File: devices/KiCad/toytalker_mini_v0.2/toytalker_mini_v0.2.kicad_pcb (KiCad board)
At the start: 2 copper layers, 40 x 40 mm, 38 parts, among them J1 TYPE-C-31-M-12, J2 SM02B-SRSS-TB(LF)(SN), U1 BQ25185DLHR, U2 AP2112K-3.3TRG1, U3 ESP32-S3-MINI-1-N4R2, U4 MAX98357AEWL_T

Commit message: Import v0.2 schematic changes into PCB and remove stale v0.1 footprints
- Update board from schematic: new connectors (ZH battery, MX1.25 speaker,
  MSK12C02 slide switch), thermistors TH1/TH2, new passives R9-R14/C10/C11
- Remove 4 ghost footprints left from v0.1: old SH connectors (J2/SP1),
  old SSAJ110100 switch, R5 (replaced by TH1)
- Keep 9 board-only speaker grille hole footprints
- File format upgraded to KiCad 10 on save

Co-Authored-By: Claude Fable 5 <noreply@anthropic.com>
Claude-Session: https://claude.ai/code/session_017Se8MNjUgWCs8o61hRDxnG
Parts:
- removed R5: 10k, Resistor_SMD:R_0402_1005Metric
- added C10: 0.1uF, Capacitor_SMD:C_0603_1608Metric, F.Cu at (68.9, 26.3)
- added C11: 0.1uF, Capacitor_SMD:C_0603_1608Metric, F.Cu at (68.9, 28.8)
- added R10: 470k, Resistor_SMD:R_0402_1005Metric, F.Cu at (55.5, 28.0)
- added R11: 470k, Resistor_SMD:R_0402_1005Metric, F.Cu at (55.5, 30.0)
- added R12: 100k, Resistor_SMD:R_0402_1005Metric, F.Cu at (55.5, 32.0)
- added R13: 100k, Resistor_SMD:R_0402_1005Metric, F.Cu at (55.5, 34.0)
- added R14: 10k, Resistor_SMD:R_0402_1005Metric, F.Cu at (55.5, 35.9)
- added R9: 100k, Resistor_SMD:R_0402_1005Metric, F.Cu at (55.5, 26.0)
- added TH1: NCP15XH103F03RC, toytalker_v02_parts:R0402, F.Cu at (72.4, 26.1)
- added TH2: NCP15XH103F03RC, toytalker_v02_parts:R0402, F.Cu at (72.4, 28.2)
- J2: value SM02B-SRSS-TB(LF)(SN) -> S2B-ZR-SM4A-TF(LF)(SN); footprint footprints:SM02B-SRSS-TB_LF__SN_ -> toytalker_v02_parts:CONN-SMD_S2B-ZR-SM4A
- R8: value 47 -> 470
- S1: value SSAJ110100 -> MSK12C02G15-B; footprint footprints:SW_SSAJ110100 -> toytalker_v02_parts:SW-SMD_MSK12C02G15-B
- S3: footprint Button_Switch_SMD:SW_SPST_B3U-1000P -> footprints:SW_B3U-1000P
- SP1: value SM02B-SRSS-TB(LF)(SN) -> HC-1.25-2PWT; footprint footprints:SM02B-SRSS-TB_LF__SN_ -> toytalker_v02_parts:CONN-SMD_2P-P1.25-HC-1.25-2PWT
- moved S1 48.9 mm to (70.9, 39.1), turned to 0 degrees
- moved J2 46.7 mm to (61.9, 29.2), turned to 0 degrees
- moved SP1 40.3 mm to (61.6, 37.0)
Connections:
- net /GPIO27 renamed /GPIO0_BOOT
- net Net-(U3-EN) renamed /ESP_EN
- C4 pad 1: /V_SYS_SW -> /V_SYS
- C9 pad 1: /+3V3 -> /V_SYS
- MK1 pad 1: /GPIO3 -> /GPIO5
- S1 pad 1: unconnected-(S1-Pad1) -> /V_SYS
- S1 pad 2: /V_SYS_SW -> /PWR_EN
- SP1 pad 3: (no net) -> unconnected-(SP1-Pad3)
- SP1 pad 4: (no net) -> unconnected-(SP1-Pad4)
- U1 pad 3: unconnected-(U1-STAT2-Pad3) -> /GPIO14
- U1 pad 9: unconnected-(U1-STAT1-Pad9) -> /GPIO13
- U2 pad 1: /V_SYS_SW -> /V_SYS
- U2 pad 3: /V_SYS_SW -> /PWR_EN
- U3 pad 14: unconnected-(U3-IO10-Pad14) -> /GPIO10
- U3 pad 15: unconnected-(U3-IO11-Pad15) -> /GPIO11
- U3 pad 16: unconnected-(U3-IO12-Pad16) -> /GPIO12
- U3 pad 17: unconnected-(U3-IO13-Pad17) -> /GPIO13
- U3 pad 18: unconnected-(U3-IO14-Pad18) -> /GPIO14
- U3 pad 5: unconnected-(U3-IO1-Pad5) -> /GPIO1
- U3 pad 6: unconnected-(U3-IO2-Pad6) -> /GPIO2
- U3 pad 7: /GPIO3 -> unconnected-(U3-IO3-Pad7)
- U4 pad A2: /+3V3 -> /V_SYS
- U4 pad B1: /GPIO5 -> /GPIO12
- U4 pad C1: /GPIO4 -> /GPIO10
- U4 pad C3: /GPIO3 -> /GPIO11
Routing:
- net /GPIO3: track 30.1 -> 0.00 mm, vias 2 -> 0
- net /GPIO5: track 26.4 -> 56.5 mm, vias 0 -> 2

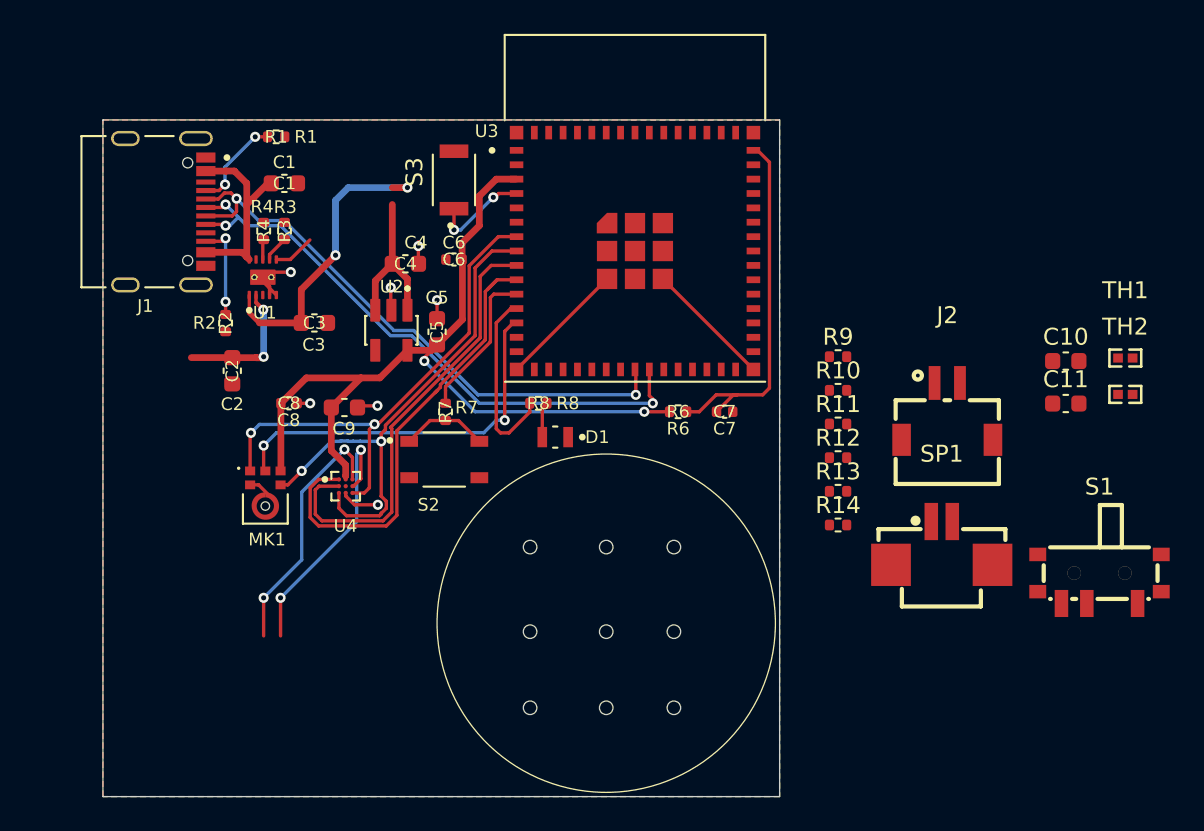
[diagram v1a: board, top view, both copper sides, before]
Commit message: Finalize v0.2 component placement: antenna in-board, bottom battery notch
- U3 rotated 270deg at (41.3,21.5): full 15.4x20.5mm module incl antenna
  inside board (right edge 0.45mm margin), 2mm routing channel on top,
  antenna strip covered by new all-layer keepout rule area
- Battery connector J2 at bottom edge facing 6x1.8mm cable notch (x25-31);
  battery mounts flipped, leads exit bottom-right (case/RFQ note)
- S1 slide switch on left edge, knob outboard; SP1 mouth toward speaker
  (connector orientations verified from pad/housing geometry)
- Thermistors stay on front side (single-side assembly, thermal vias later)
- Monitoring passives moved to old J2 area on left edge; C6 in top channel
- DRC: courtyard overlaps 0, copper-edge violations 0 (routing cleanup next)

Co-Authored-By: Claude Fable 5 <noreply@anthropic.com>
Claude-Session: https://claude.ai/code/session_017Se8MNjUgWCs8o61hRDxnG
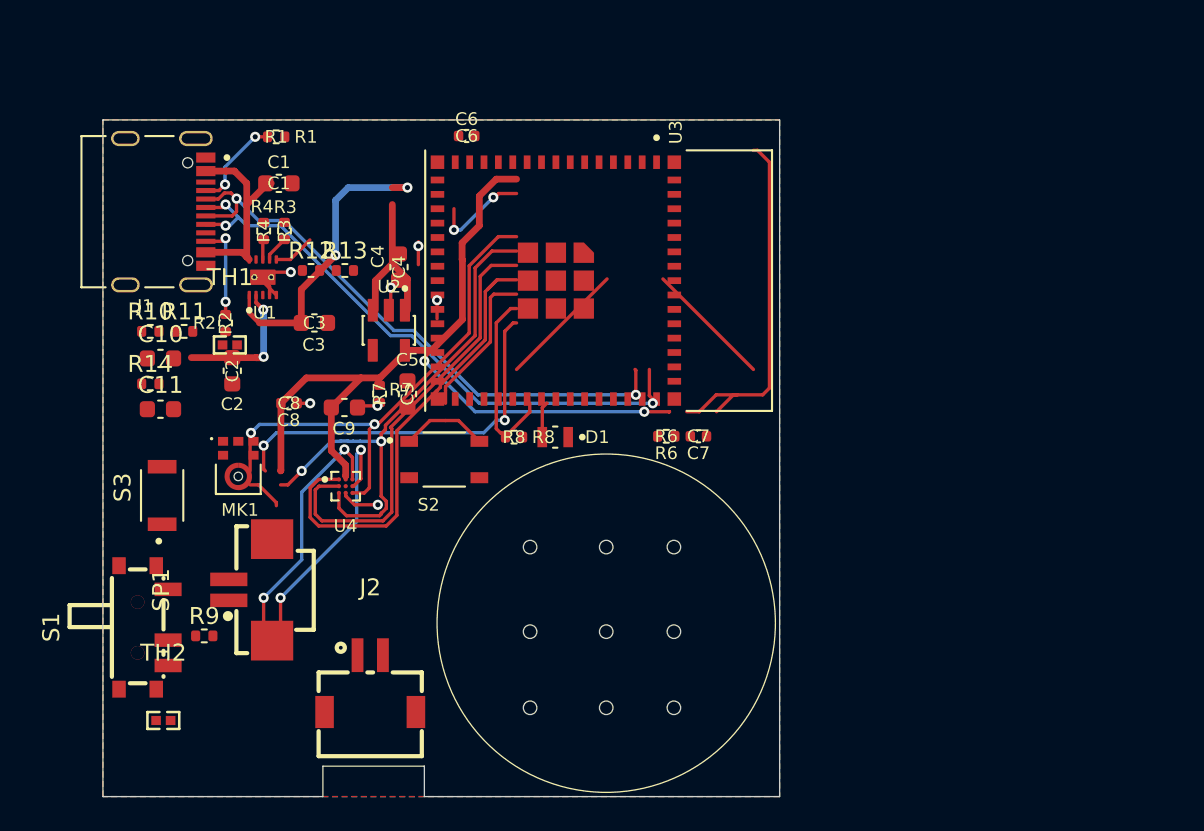
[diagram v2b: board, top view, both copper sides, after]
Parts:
- moved TH2 60.0 mm to (15.6, 47.5)
- moved S1 56.6 mm to (14.4, 42.0), turned to 90 degrees
- moved C11 53.5 mm to (15.4, 29.1)
- moved C10 53.5 mm to (15.4, 26.1)
- moved TH1 52.9 mm to (19.5, 25.3)
- moved R14 41.5 mm to (14.8, 27.6)
- moved SP1 41.0 mm to (20.7, 39.8), turned to 90 degrees
- moved R9 40.9 mm to (18.0, 42.5)
- moved R10 40.8 mm to (14.8, 24.5)
- moved R11 39.0 mm to (16.8, 24.5)
- moved J2 37.7 mm to (27.8, 45.3)
- moved R12 33.1 mm to (24.3, 20.9)
- moved R13 31.9 mm to (26.3, 20.9)
- moved S3 25.4 mm to (15.5, 34.2)
- moved C6 7.34 mm to (33.5, 12.9)
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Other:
- outline, holes or cut-outs redrawn

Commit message: Move LED to IO40; placement QA complete, all decap distances pass
- LED reassigned IO47->IO40 (bottom row): IO47's west path to R8 was
  blocked by C9/S2/MK1 gaps (3 routes checked); IO40 rides the S2-east
  lane with the amp bundle, no B-side jump needed
- ERC 0/0, netlist verified: /GPIO40={R8-2,U3-36}, GPIO47 eliminated
- User rework: C1 to 2.2mm from U1.IN with VBUS reroute, C2 4.1mm,
  CC resistors tucked to J1, TH1 relocated away from charger heat
  (19mm, fixes self-heating false charge-stop), TH2 near module kept
  as deliberate ESP32-area sensor (paired with internal die sensor)
- Fixed C10/C11 footprint symbol-link corruption from earlier template
  copy (duplicate C6/C11 removed, links repaired)

Co-Authored-By: Claude Fable 5 <noreply@anthropic.com>
Claude-Session: https://claude.ai/code/session_017Se8MNjUgWCs8o61hRDxnG
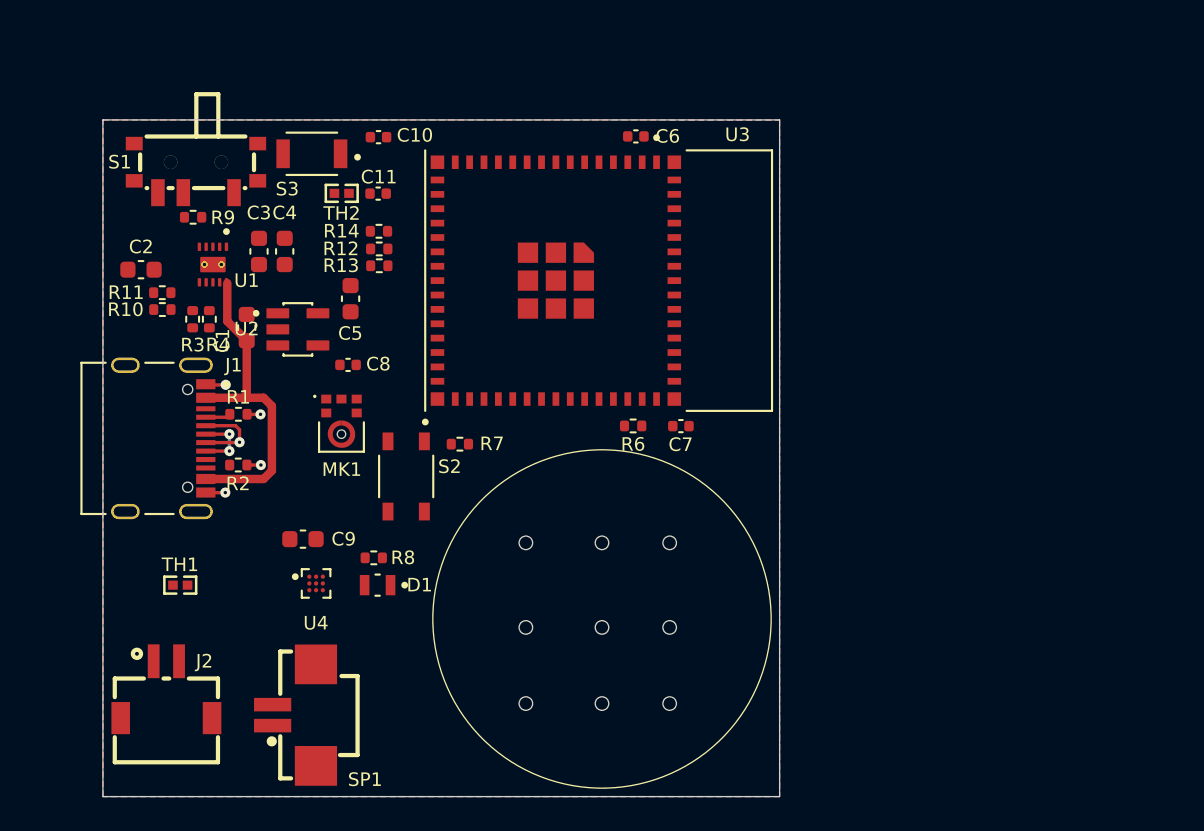
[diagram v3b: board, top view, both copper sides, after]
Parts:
- C10, C11: footprint Capacitor_SMD:C_0603_1608Metric -> Capacitor_SMD:C_0402_1005Metric
- moved TH2 32.9 mm to (26.1, 16.3), turned to 180 degrees
- moved S1 27.3 mm to (17.5, 14.8), turned to 0 degrees
- moved R9 24.8 mm to (17.3, 17.8)
- moved S3 22.1 mm to (24.3, 14.0), turned to 180 degrees
- moved C10 18.4 mm to (28.3, 13.0)
- moved C11 18.1 mm to (28.3, 16.4)
- moved R1 16.6 mm to (20.0, 29.4)
- moved R14 16.2 mm to (28.3, 18.6)
- moved TH1 14.5 mm to (16.6, 39.5), turned to 180 degrees
- moved D1 13.7 mm to (28.2, 39.5)
- moved J1 13.4 mm to (13.3, 30.8)
- moved J2 12.1 mm to (15.8, 45.7)
- moved R8 10.9 mm to (28.0, 37.9), turned to 0 degrees
- moved C6 10.0 mm to (43.5, 13.0), turned to 0 degrees
- moved C1 8.73 mm to (20.5, 24.3), turned to 90 degrees
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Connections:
- MK1 pad 1: /GPIO5 -> /GPIO33
- MK1 pad 4: /GPIO4 -> /GPIO48
- MK1 pad 6: /GPIO9 -> /GPIO34
- R7 pad 2: /GPIO7 -> /GPIO35
- R8 pad 2: /GPIO8 -> /GPIO47
- U3 pad 10: /GPIO6 -> unconnected-(U3-IO6-Pad10)
- U3 pad 11: /GPIO7 -> unconnected-(U3-IO7-Pad11)
- U3 pad 12: /GPIO8 -> unconnected-(U3-IO8-Pad12)
- U3 pad 13: /GPIO9 -> unconnected-(U3-IO9-Pad13)
- U3 pad 14: /GPIO10 -> unconnected-(U3-IO10-Pad14)
- U3 pad 15: /GPIO11 -> unconnected-(U3-IO11-Pad15)
- U3 pad 16: /GPIO12 -> unconnected-(U3-IO12-Pad16)
- U3 pad 27: unconnected-(U3-IO47-Pad27) -> /GPIO47
- U3 pad 28: unconnected-(U3-IO33-Pad28) -> /GPIO33
- U3 pad 29: unconnected-(U3-IO34-Pad29) -> /GPIO34
- U3 pad 30: unconnected-(U3-IO48-Pad30) -> /GPIO48
- U3 pad 31: unconnected-(U3-IO35-Pad31) -> /GPIO35
- U3 pad 32: unconnected-(U3-IO36-Pad32) -> /GPIO36
- U3 pad 33: unconnected-(U3-IO37-Pad33) -> /GPIO37
- U3 pad 34: unconnected-(U3-IO38-Pad34) -> /GPIO38
- U3 pad 35: unconnected-(U3-IO39-Pad35) -> /GPIO39
- U3 pad 8: /GPIO4 -> unconnected-(U3-IO4-Pad8)
- U3 pad 9: /GPIO5 -> unconnected-(U3-IO5-Pad9)
- U4 pad A1: /GPIO6 -> /GPIO39
- U4 pad B1: /GPIO12 -> /GPIO38
- U4 pad C1: /GPIO10 -> /GPIO36
- U4 pad C3: /GPIO11 -> /GPIO37
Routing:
- net /GPIO5: track 56.5 -> 0.00 mm, vias 2 -> 0
- net /+3V3: track 51.0 -> 0.00 mm, vias 2 -> 0
- net /GPIO20: track 35.6 -> 3.79 mm, vias 3 -> 2
- net /GPIO4: track 30.6 -> 0.00 mm, vias 2 -> 0
- net /GPIO19: track 34.7 -> 4.84 mm, vias 2 -> 1
- net /GPIO6: track 27.7 -> 0.00 mm
- net GND: track 28.6 -> 3.39 mm, vias 7 -> 4
- net /GPIO9: track 22.6 -> 0.00 mm, vias 2 -> 0
- net /ESP_EN: track 21.7 -> 0.00 mm
- net /V_SYS: track 17.7 -> 0.00 mm, vias 2 -> 0
- net /OUTN: track 15.4 -> 0.00 mm, vias 2 -> 0
- net /OUTP: track 15.0 -> 0.00 mm, vias 2 -> 0
- net /GPIO8: track 10.9 -> 0.00 mm
- net /V_SYS_SW: track 9.65 -> 0.00 mm
- net /GPIO7: track 8.98 -> 0.00 mm
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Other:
- outline, holes or cut-outs redrawn

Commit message: Complete v0.2 routing: all nets routed, GND fully stitched, DRC clean
- All 66 nets routed (user hand-routing + planned B-side jumps, all
  west of module; ESP32 underside and antenna B.Cu kept pristine)
- GND infrastructure: 9-via thermal farm under ESP32 (datasheet land
  pattern), 4 antenna-side stitch vias (Espressif HW guideline), solid
  zone connects on U3/U1/MK1/J1, U1 thermal holes net-assigned,
  TH1/TH2 thermal vias, 20+ stitch vias for isolated pour pockets
- Fixed 4 isolated GND clusters found by union-find connectivity
  analysis (incl. U1 charger group fenced in by B-side jumps; final
  link found by BFS maze-solver on B.Cu)
- Legacy v0.1 antenna keepouts stranded off-board inside U3 footprint
  removed; via standards normalized via netclasses (0.5/0.3, pwr 0.6/0.3)
- Remaining DRC items are known-benign only (connector-at-edge, WLP
  mask slivers, switch peg annulars, silk cosmetics)

Co-Authored-By: Claude Fable 5 <noreply@anthropic.com>
Claude-Session: https://claude.ai/code/session_017Se8MNjUgWCs8o61hRDxnG
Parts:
- moved U4 4.10 mm to (25.5, 35.4), turned to 90 degrees
- moved C9 2.12 mm to (22.2, 35.4)
- moved C10 1.70 mm to (29.4, 14.3), turned to 180 degrees
- moved TH2 1.49 mm to (25.2, 17.5), turned to -90 degrees
- moved R9 1.40 mm to (18.2, 16.7)
- moved C2 1.35 mm to (14.3, 19.5)
- moved C11 1.12 mm to (29.2, 15.8), turned to 180 degrees
- moved R12 1.05 mm to (27.5, 19.0)
- moved R13 1.05 mm to (27.5, 20.0)
- moved R14 1.05 mm to (27.5, 18.0)
- moved R7 0.77 mm to (32.7, 30.5), turned to 90 degrees
- moved R11 0.74 mm to (16.0, 21.6), turned to 90 degrees
- moved U2 0.53 mm to (24.1, 24.4), turned to -90 degrees
- moved R8 0.52 mm to (27.5, 38.0)
- moved S2 0.50 mm to (29.9, 32.6)
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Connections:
- R8 pad 2: /GPIO47 -> /GPIO40
- U1 pad 12: (no net) -> GND
- U1 pad 13: (no net) -> GND
- U3 pad 27: /GPIO47 -> unconnected-(U3-IO47-Pad27)
- U3 pad 36: unconnected-(U3-IO40-Pad36) -> /GPIO40
- U4 pad C1: /GPIO36 -> /GPIO37
- U4 pad C3: /GPIO37 -> /GPIO36
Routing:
- net GND: track 3.39 -> 57.9 mm, vias 4 -> 32
- net /+3V3: track 0.00 -> 54.4 mm, vias 0 -> 2
- net /GPIO1: track 0.00 -> 35.3 mm, vias 0 -> 4
- net /V_SYS: track 0.00 -> 32.3 mm
- net /VBAT: track 0.00 -> 29.6 mm, vias 0 -> 2
- net /GPIO14: track 0.00 -> 21.6 mm, vias 0 -> 2
- net /OUTP: track 0.00 -> 20.4 mm, vias 0 -> 2
- net Net-(U1-TS/MR): track 0.00 -> 19.3 mm, vias 0 -> 2
- net /GPIO13: track 0.00 -> 18.8 mm, vias 0 -> 2
- net /GPIO2: track 0.00 -> 18.7 mm, vias 0 -> 2
- net /OUTN: track 0.00 -> 18.0 mm, vias 0 -> 2
- net /GPIO0_BOOT: track 0.00 -> 17.8 mm, vias 0 -> 2
- net /GPIO39: track 0.00 -> 17.1 mm
- net /GPIO20: track 3.79 -> 20.4 mm, vias 2 -> 3
- net /GPIO19: track 4.84 -> 21.0 mm, vias 1 -> 2
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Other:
- outline, holes or cut-outs redrawn

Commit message: Final GND QA pass: solid connects on S3/R9, cleanup, all audits green
- S3/R9 pads set to solid zone connection (last starved-thermal items)
- Redundant via + stub near S3 removed (leftover from two-pass fix)
- Full QA verified: unconnected 0, schematic parity clean (17 hits =
  9 board-only speaker holes, 2 = intentional U1 thermal-hole GND),
  B.Cu sanctuary clean, antenna strip clean, decap distances pass,
  via ledger 64 vias all accounted (farm 9 / antenna 4 / stitch 18 /
  signal layer-changes 33 in consistent pairs)
- Remaining 25 DRC items all triaged benign (documented); exclusion
  marking deferred to pre-order checklist

Co-Authored-By: Claude Fable 5 <noreply@anthropic.com>
Claude-Session: https://claude.ai/code/session_017Se8MNjUgWCs8o61hRDxnG
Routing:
- net GND: track 57.9 -> 57.5 mm, vias 32 -> 31
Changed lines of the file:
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@@
 		(tags "capacitor")
 		(property "Reference" "C1"
-			(at -0.775 -1.408089 90)
+			(at -2.075 0.9 180)
 			(layer "F.SilkS")
 			(effects
@@
 		(tags "capacitor")
 		(property "Reference" "C9"
-			(at -2.412632 -0.005427 0)
+			(at -0.003765 -1.427931 0)
 			(layer "F.SilkS")
 			(effects
@@
 		(tags "resistor")
 		(property "Reference" "R6"
-			(at 0.001763 -1.093816 0)
+			(at 1.640745 -0.760366 0)
 			(layer "F.SilkS")
 			(effects
@@
 			)
 		)
+		(zone_connect 2)
 		(attr smd)
 		(duplicate_pad_numbers_are_jumpers no)
@@
 			)
 		)
+		(zone_connect 2)
 		(attr smd)
 		(duplicate_pad_numbers_are_jumpers no)
@@
 		(tags "capacitor")
 		(property "Reference" "C6"
-			(at 1.888702 0 0)
+			(at 2.197903 0.024713 0)
 			(layer "F.SilkS")
 			(effects
@@
 		(tags "capacitor")
 		(property "Reference" "C7"
-			(at -0.007934 1.097557 180)
+			(at 1.73518 -0.000682 180)
 			(layer "F.SilkS")
 			(effects
@@
 	)
 	(segment
+		(start 26.079006 17.930994)
+		(end 26.08 17.93)
+		(width 0.2)
+		(layer "F.Cu")
+		(net "GND")
+	)
+	(segment
 		(start 45.775 14.5)
 		(end 45.85 14.5)
@@
 	)
 	(segment
+		(start 25.179686 17.930994)
+		(end 26.079006 17.930994)
+		(width 0.2)
+		(layer "F.Cu")
+		(net "GND")
+	)
+	(segment
 		(start 21.314788 29.405401)
 		(end 20.525401 29.405401)
@@
 	)
 	(segment
-		(start 22.649 14.003)
-		(end 22.85 12.75)
-		(width 0.25)
-		(layer "F.Cu")
-		(net "GND")
-	)
-	(segment
 		(start 18.3 24.303134)
 		(end 18.3 25.15)
@@
 	)
 	(via
-		(at 23.72 12.82)
+		(at 24.35 14)
 		(size 0.5)
 		(drill 0.3)
@@
 		(size 0.5)
 		(drill 0.3)
-		(layers "F.Cu" "B.Cu")
-		(net "GND")
-	)
-	(via
-		(at 22.85 12.75)
-		(size 0.5)
-		(drill 0.3)
